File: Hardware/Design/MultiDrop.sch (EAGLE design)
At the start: 36 parts

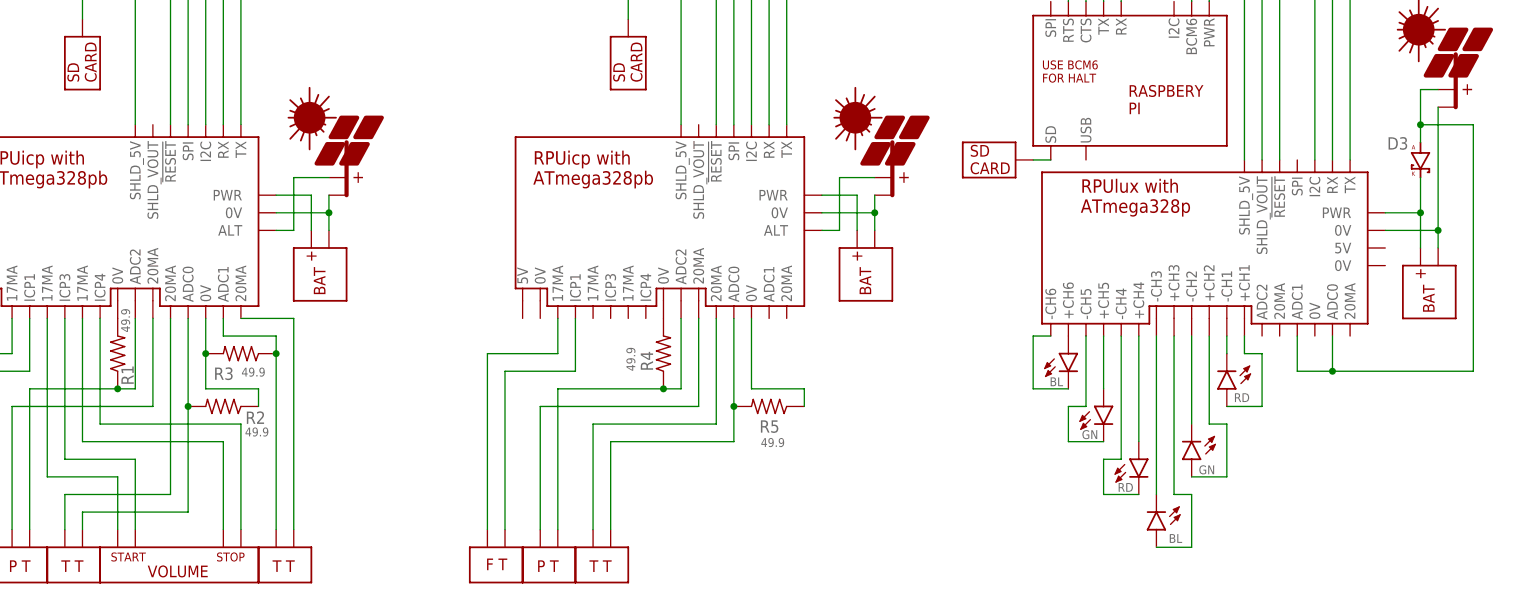
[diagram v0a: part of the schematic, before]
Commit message: Hardware: ^0 review, PWR_I sense, SHLD_VIN gate stress
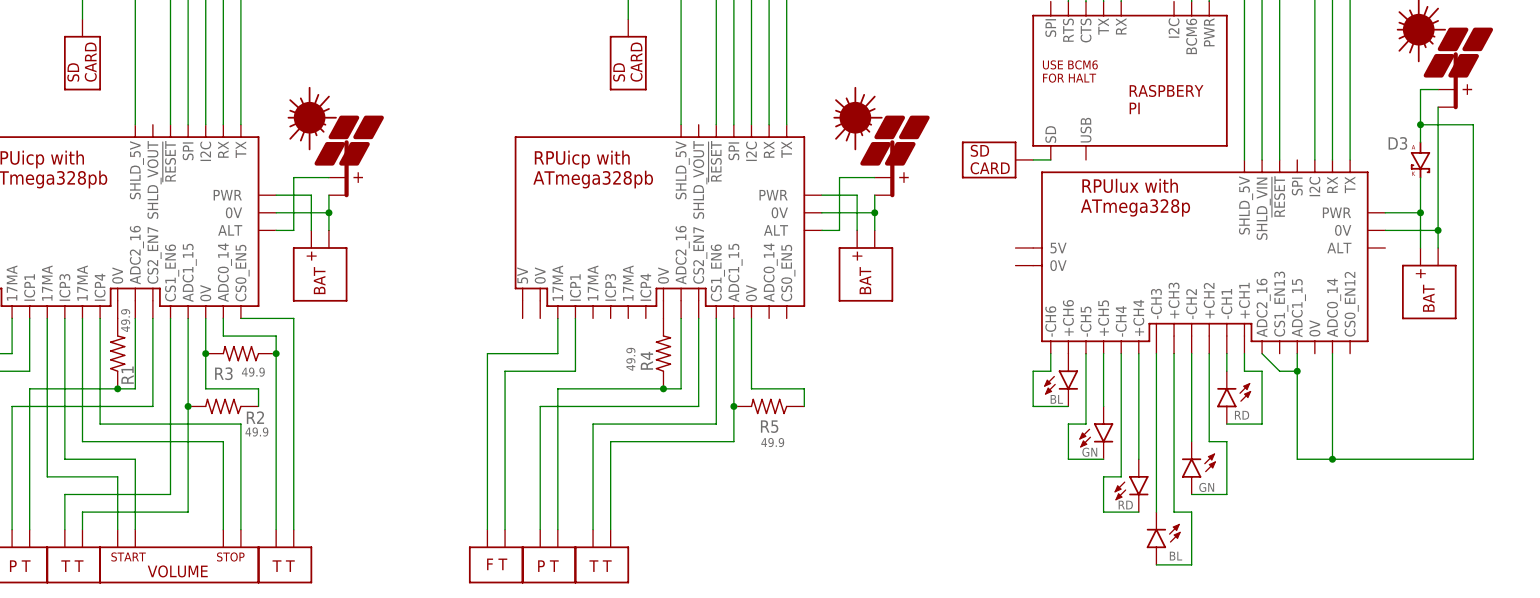
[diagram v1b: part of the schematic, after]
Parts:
- removed U$8: RPULUX, Documentation:RPULUX
- added U$19: RPULUX, Documentation:RPULUX
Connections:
- removed net N$64: RD1.K, U$8.-CH1
- new net N$62: RD1.K, U$19.-CH1
- net N$13: now also U$19.SHLD_5V; no longer U$8.SHLD_5V
- net N$14: now also U$19.TX; no longer U$8.TX
- net N$15: now also U$19.PWR; no longer U$8.PWR
- net N$16: now also U$19.ADC0_14, U$19.ADC1_15, U$19.ADC2_16; no longer U$8.ADC0, U$8.ADC1
- net N$21: now also U$19.RX; no longer U$8.RX
- net N$25: now also U$19.+CH6; no longer U$8.+CH6
- net N$31: now also U$6.CS0_EN5; no longer U$6.20MA@1
- net N$32: now also U$19.I2C; no longer U$8.I2C
- net N$34: now also U$6.ADC0_14; no longer U$6.ADC1
- net N$35: now also U$6.ADC1_15; no longer U$6.ADC0
- net N$36: now also U$6.CS1_EN6; no longer U$6.20MA@0
- net N$37: now also U$6.ADC2_16; no longer U$6.ADC2
- net N$40: now also U$19.+CH4; no longer U$8.+CH4
- net N$41: now also U$19.SHLD_VIN; no longer U$8.SHLD_VOUT
- net N$42: now also U$19.0V@2; no longer U$8.0V@2
- net N$43: now also U$19.!RESET; no longer U$8.!RESET
- net N$46: now also U$19.-CH4; no longer U$8.-CH4
- net N$47: now also U$19.+CH5; no longer U$8.+CH5
- net N$49: now also U$19.-CH5; no longer U$8.-CH5
- net N$50: now also U$6.CS2_EN7; no longer U$6.20MA@2
- net N$51: now also U$19.-CH6; no longer U$8.-CH6
- net N$56: now also U$5.ADC2_16; no longer U$5.ADC2
- net N$57: now also U$5.CS2_EN7; no longer U$5.20MA@2
- net N$58: now also U$5.ADC1_15; no longer U$5.ADC0
- net N$59: now also U$5.CS1_EN6; no longer U$5.20MA@0
- net N$65: now also U$19.+CH1; no longer U$8.+CH1
- net N$66: now also U$19.+CH2; no longer U$8.+CH2
- net N$67: now also U$19.-CH2; no longer U$8.-CH2
- net N$68: now also U$19.+CH3; no longer U$8.+CH3
- net N$69: now also U$19.-CH3; no longer U$8.-CH3
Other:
- note added: "13AHr"
- note added: "50AHr"
- note added: "SLP020-12U"
- note added: "SLP070-12U"

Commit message: Hardware: ^0 reviewing
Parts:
- removed D3: (no value), D-SBR:DSMB
- added U$8: SSR_DC, Documentation:SSR_DC
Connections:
- new net N$63: PV4.+PV, U$19.ADC2_16, U$8.+DC
- new net N$64: U$19.PWR, U$7.+BAT, U$8.+IN, U$8.-DC
- net +DTR: now also U$1.+DTR; no longer U$4.+DTR
- net +DTR3: now also U$4.+DTR; no longer U$1.+DTR
- net +RX: now also U$1.+RX; no longer U$4.+RX
- net +RX3: now also U$4.+RX; no longer U$1.+RX
- net +TX: now also U$1.+TX; no longer U$4.+TX
- net +TX3: now also U$4.+TX; no longer U$1.+TX
- net -DTR: now also U$1.-DTR; no longer U$4.-DTR
- net -DTR3: now also U$4.-DTR; no longer U$1.-DTR
- net -RX: now also U$1.-RX; no longer U$4.-RX
- net -RX3: now also U$4.-RX; no longer U$1.-RX
- net -TX: now also U$1.-TX; no longer U$4.-TX
- net -TX3: now also U$4.-TX; no longer U$1.-TX
- net N$1: now also U$1.BM_TX; no longer U$4.BM_TX
- net N$12: now also U$4.SHDN; no longer U$1.DIO8
- net N$13: now also U$4.PWR; no longer U$1.PWR
- net N$14: now also U$4.BM_TX; no longer U$1.BM_TX
- net N$15: now also U$3.I2C, U$4.I2C1; no longer D3.K, U$19.PWR, U$7.+BAT
- net N$16: now also U$8.-IN; no longer D3.A, PV4.+PV, U$19.ADC1_15, U$19.ADC2_16
- net N$2: now also U$1.BM_RX; no longer U$4.BM_RX
- net N$21: now also U$4.BM_RX; no longer U$1.BM_RX
- net N$22: now also U$4.!CTS; no longer U$1.!CTS
- net N$23: now also U$4.!RTS; no longer U$1.!RTS
- net N$26: now also U$4.HOST_RX; no longer U$1.HOST_RX
- net N$27: now also U$4.HOST_TX; no longer U$1.HOST_TX
- net N$29: now also U$1.PWR; no longer U$4.PWR
- net N$30: now also U$1.BM-!RST!; no longer U$4.DIO10
- net N$32: now also U$4.I2C0; no longer U$1.I2C
- net N$33: now also U$1.I2C0; no longer U$4.I2C
- net N$43: now also U$4.BM-!RST!; no longer U$1.DIO10
- net N$44: now also U$2.BM-!RST!; no longer U$2.DIO10
- net N$48: now also U$2.I2C0; no longer U$2.I2C

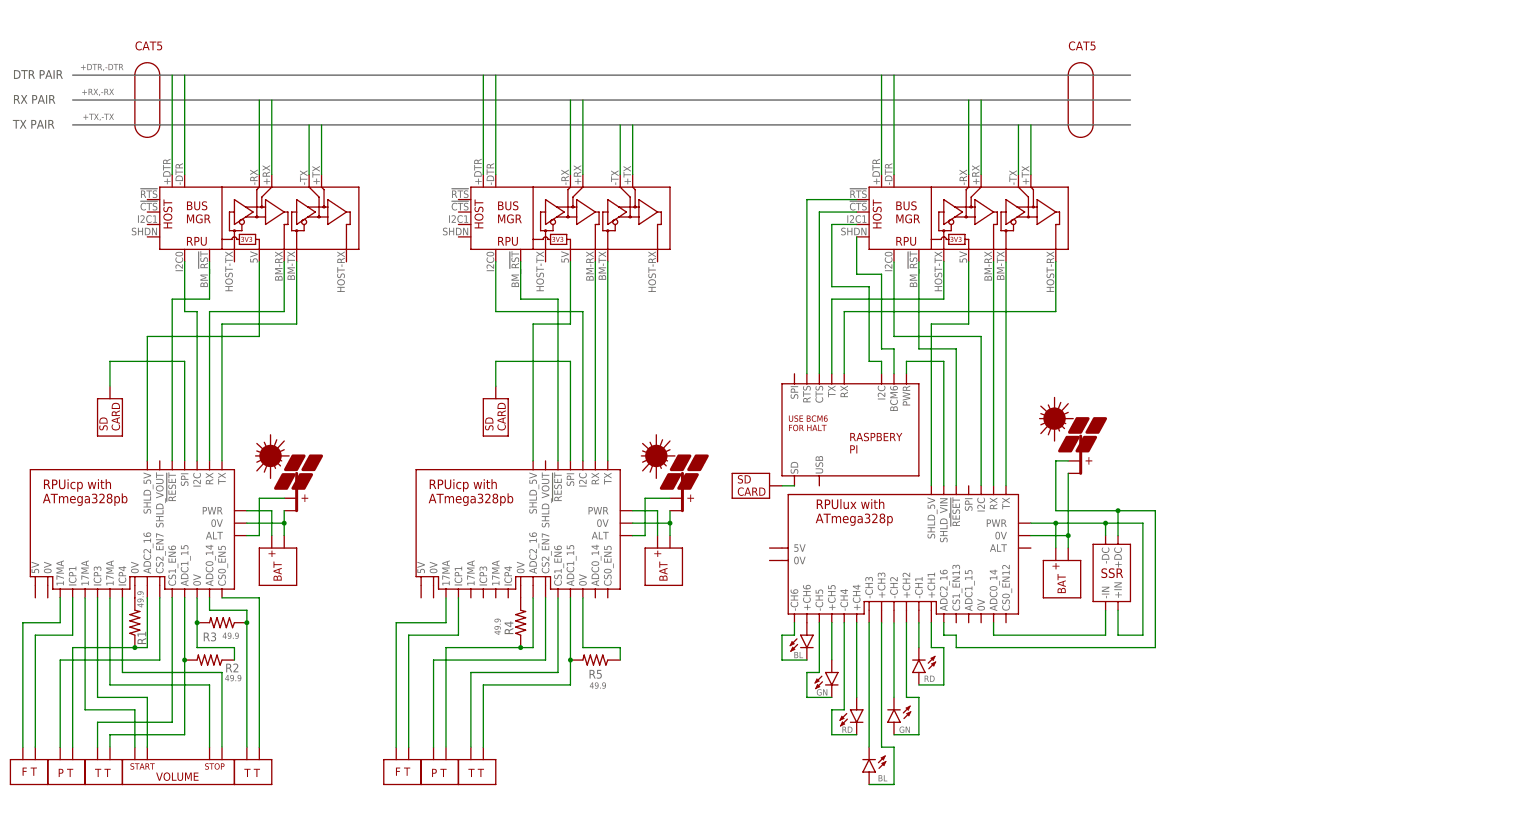
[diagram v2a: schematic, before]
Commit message: Hardware: overview, 1mSec one-shot, nSS to nCE00
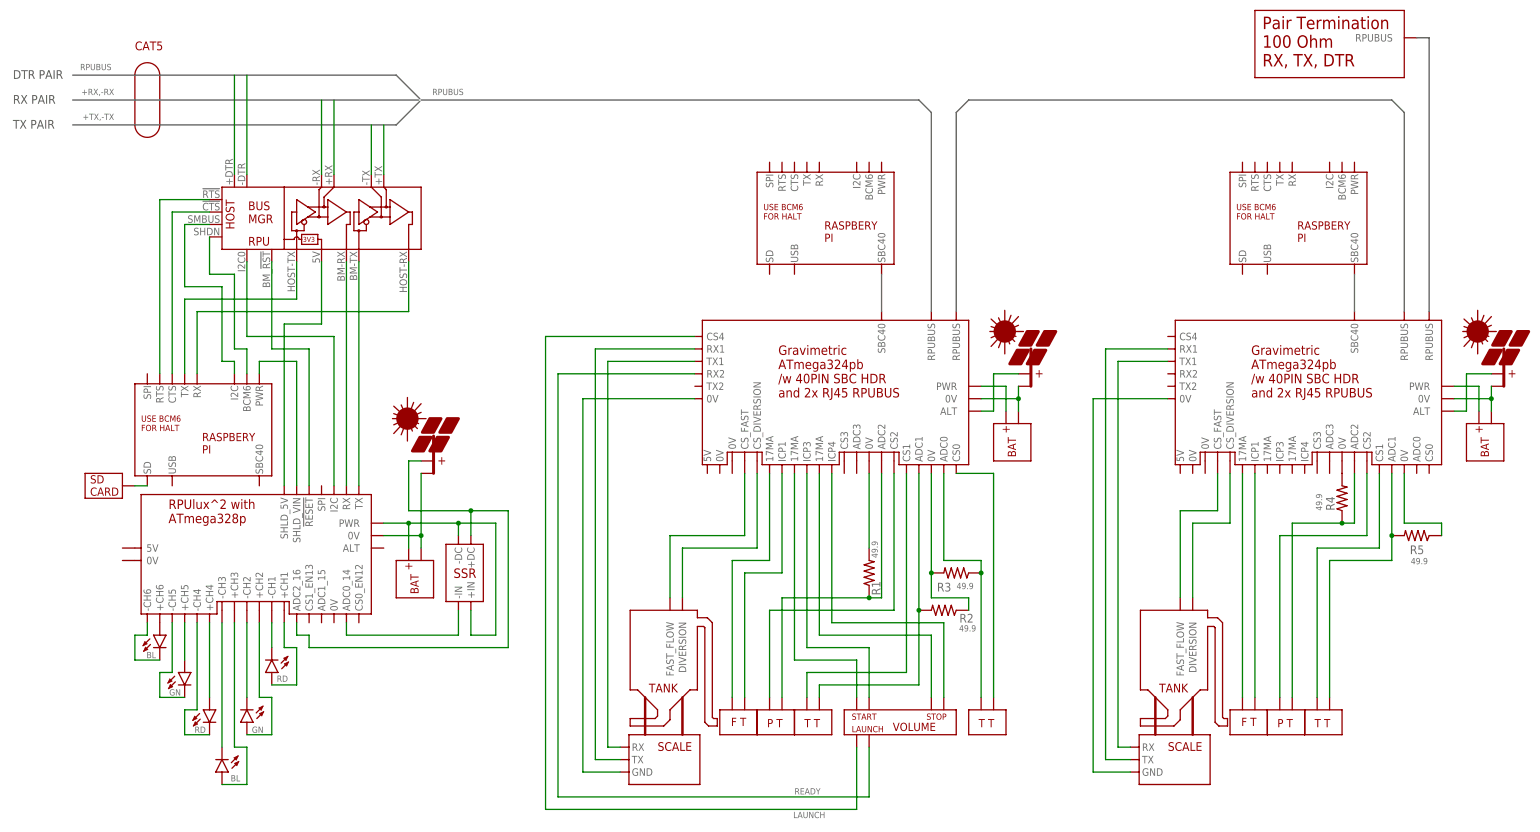
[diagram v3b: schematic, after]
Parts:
- removed SD1, SD3: SD, Documentation:SD
- added U$20: PI, Documentation:PI
- added U$21, U$22: SCALE, Documentation:SCALE
- U$1, U$2: value BUS_MGR -> GRAVIMETRIC; device Documentation:BUS_MGR -> Documentation:GRAVIMETRIC
- U$5: value RPUICP -> TERM; device Documentation:RPUICP -> Documentation:TERM
- U$6: value RPUICP -> PI; device Documentation:RPUICP -> Documentation:PI
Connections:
- removed net +DTR: U$1.+DTR
- removed net +DTR1: U$2.+DTR
- removed net +RX: U$1.+RX
- removed net +RX1: U$2.+RX
- removed net +TX: U$1.+TX
- removed net +TX1: U$2.+TX
- removed net -DTR: U$1.-DTR
- removed net -DTR1: U$2.-DTR
- removed net -RX: U$1.-RX
- removed net -RX1: U$2.-RX
- removed net -TX: U$1.-TX
- removed net -TX1: U$2.-TX
- removed net N$52: R1.2, U$6.0V@4
- removed net N$60: R4.2, U$5.0V@4
- new net LAUNCH: U$1.CS4, U$15.LAUNCH
- new net READY: U$1.RX2, U$15.READY
- net N$1: now also R1.2, U$1.0V@4; no longer U$1.BM_TX, U$6.TX
- net N$10: now also U$1.CS_FAST, U$21.FAST_FLOW; no longer U$2.BM_TX, U$5.TX
- net N$11: now also U$1.TX1, U$21.RX; no longer U$2.BM_RX, U$5.RX
- net N$15: now also U$4.SMBUS; no longer U$4.I2C1
- net N$17: now also U$1.RX1, U$21.TX; no longer SD1.PV_PWR, U$5.SPI
- net N$18: now also U$2.PWR; no longer U$5.PWR
- net N$19: now also U$2.ALT; no longer U$5.ALT
- net N$2: now also R4.2, U$2.0V@4; no longer U$1.BM_RX, U$6.RX
- net N$20: now also U$1.17MA@4, U$15.STOP; no longer U$15.PWR_STP, U$6.17MA@4
- net N$24: now also U$1.ICP4, U$15.STOP_RTN; no longer U$15.STOP_LOOP, U$6.ICP4
- net N$29: now also U$1.0V@6, U$21.GND; no longer U$1.PWR, U$6.SHLD_5V
- net N$3: now also U$1.ALT; no longer U$6.ALT
- net N$30: now also U$2.CS_DIVERSION, U$22.DIVERSION; no longer U$1.BM-!RST!, U$6.!RESET
- net N$31: now also U$1.CS0; no longer U$6.CS0_EN5
- net N$33: now also U$2.CS_FAST, U$22.FAST_FLOW; no longer U$1.I2C0, U$6.I2C
- net N$34: now also U$1.ADC0; no longer U$6.ADC0_14
- net N$35: now also U$1.ADC1; no longer U$6.ADC1_15
- net N$36: now also U$1.CS1; no longer U$6.CS1_EN6
- net N$37: now also U$1.ADC2; no longer U$6.ADC2_16
- net N$38: now also U$1.0V@2; no longer U$6.0V@2
- net N$39: now also U$2.0V@2; no longer U$5.0V@2
- net N$4: now also U$1.PWR; no longer U$6.PWR
- net N$44: now also U$2.TX1, U$22.RX; no longer U$2.BM-!RST!, U$5.!RESET
- net N$45: now also U$2.RX1, U$22.TX; no longer U$2.PWR, U$5.SHLD_5V
- net N$48: now also U$2.0V@6, U$22.GND; no longer U$2.I2C0, U$5.I2C
- net N$5: now also U$1.CS_DIVERSION, U$21.DIVERSION; no longer SD3.PV_PWR, U$6.SPI
- net N$50: now also U$1.CS2; no longer U$6.CS2_EN7
- net N$53: now also U$1.0V@3; no longer U$6.0V@3
- net N$54: now also U$2.17MA@1; no longer U$5.17MA@1
- net N$55: now also U$2.ICP1; no longer U$5.ICP1
- net N$56: now also U$2.ADC2; no longer U$5.ADC2_16
- net N$57: now also U$2.CS2; no longer U$5.CS2_EN7
- net N$58: now also U$2.ADC1; no longer U$5.ADC1_15
- net N$59: now also U$2.CS1; no longer U$5.CS1_EN6
- net N$6: now also U$1.17MA@1; no longer U$6.17MA@1
- net N$61: now also U$2.0V@3; no longer U$5.0V@3
- net N$7: now also U$1.ICP1; no longer U$6.ICP1
- net N$8: now also U$1.17MA@3, U$15.START; no longer U$15.PWR_STR, U$6.17MA@3
- net N$9: now also U$1.ICP3, U$15.STAR_RTN; no longer U$15.STAR_LOOP, U$6.ICP3
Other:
- note added: "GRAVIMETRIC CALIBRATION OF FLOW METER"
- note added: "GRAVIMETRIC CALIBRATION OF FLOW METER AND VOLUME"
- note added: "RJ45"
- note removed: "CALIBRATION METER"
- note removed: "PRODUCTION METER"
- note removed: "RPUadpt"
- moved on the sheet: R1, R2, R3, R4, R5
